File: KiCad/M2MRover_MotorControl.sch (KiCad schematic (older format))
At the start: 23 parts, among them J12 Screw_Terminal_01x02, J13 Screw_Terminal_01x02, SW1 SW_SPST, U3 L298HN

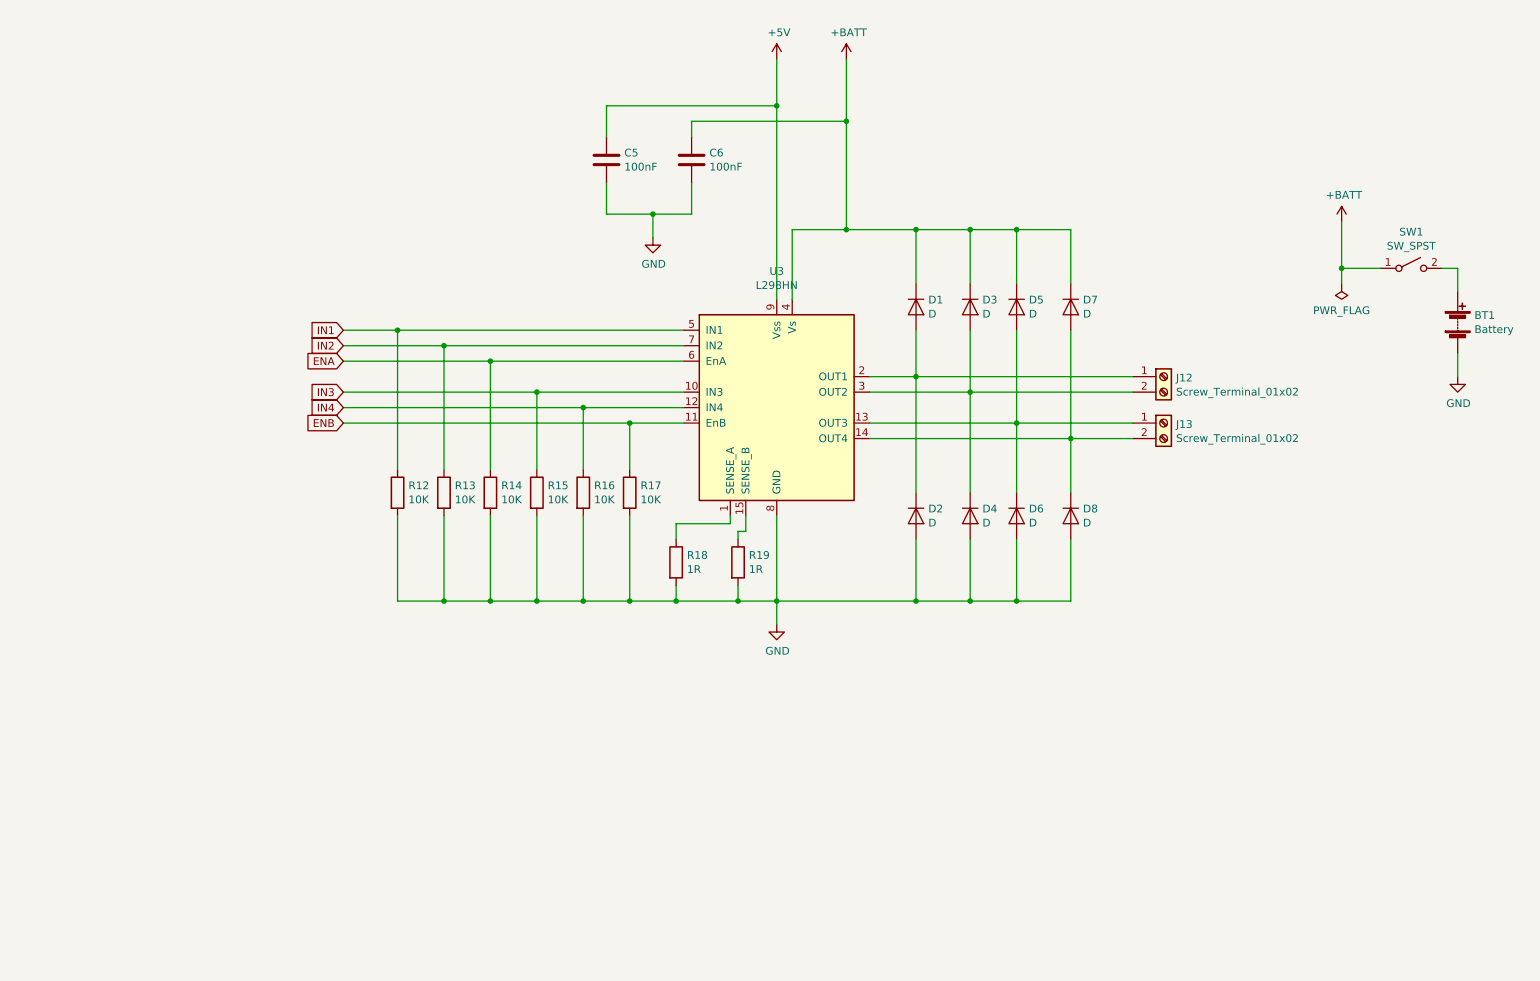
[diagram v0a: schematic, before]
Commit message: Add L298N H-Bridge driver
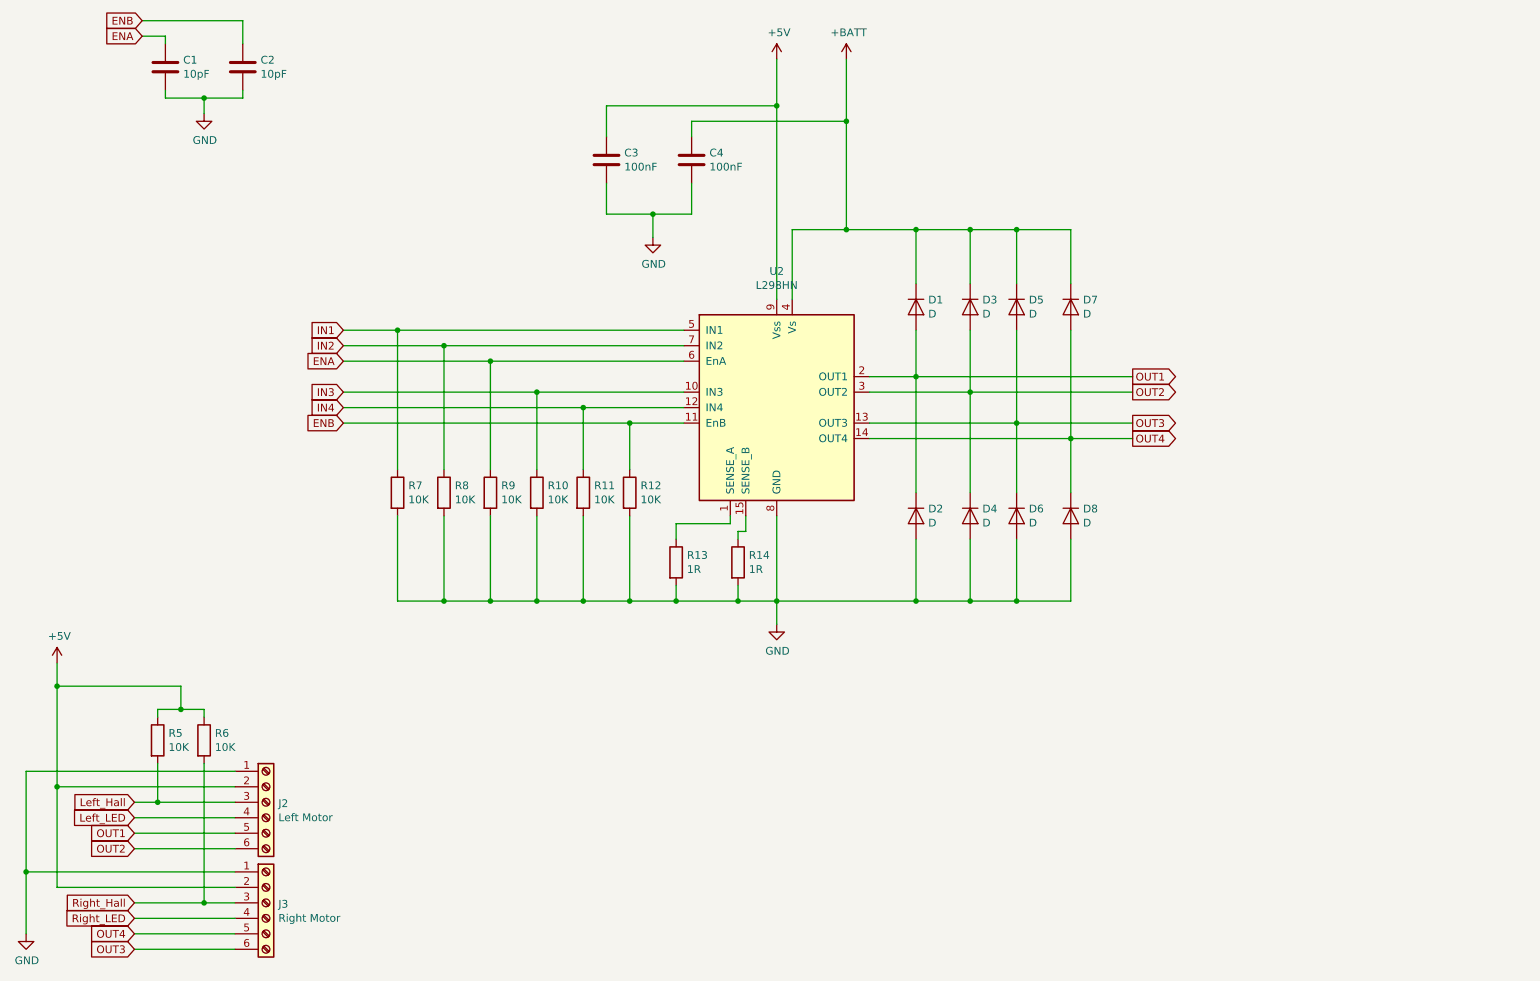
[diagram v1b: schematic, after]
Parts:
- removed BT1: Battery, symbol Device:Battery
- removed J12, J13: Screw_Terminal_01x02, symbol Connector:Screw_Terminal_01x02
- removed SW1: SW_SPST, symbol Switch:SW_SPST
- added C1, C2: 10pF, Capacitor_SMD:C_0805_2012Metric_Pad1.15x1.40mm_HandSolder, symbol Device:C
- added J2: Left Motor, Connector_PinSocket_2.54mm:PinSocket_1x06_P2.54mm_Vertical, symbol Connector:Screw_Terminal_01x06
- added J3: Right Motor, Connector_PinSocket_2.54mm:PinSocket_1x06_P2.54mm_Vertical, symbol Connector:Screw_Terminal_01x06
- added R5, R6: 10K, Resistor_SMD:R_0805_2012Metric_Pad1.15x1.40mm_HandSolder, symbol Device:R
- C3: renamed from C5; footprint (none) -> Capacitor_SMD:C_0805_2012Metric_Pad1.15x1.40mm_HandSolder
- C4: renamed from C6; footprint (none) -> Capacitor_SMD:C_0805_2012Metric_Pad1.15x1.40mm_HandSolder
- renumbered R15 to R10, R16 to R11, R17 to R12, R18 to R13, R19 to R14, R12 to R7, R13 to R8, R14 to R9, U3 to U2
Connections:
- net +5V: now also J2.2 (Pin_2), J3.2 (Pin_2), R5.1, R6.1
- net ENA: now also C1.1
- net ENB: now also C2.1
- net GND: now also C1.2, C2.2, J2.1 (Pin_1), J3.1 (Pin_1)
- net OUT3: now reaches D5.2 (A), D6.1 (K), U2.13 (OUT3)
- net OUT3: now also J3.6 (Pin_6)
- net OUT4: now reaches D7.2 (A), D8.1 (K), U2.14 (OUT4)
- net OUT4: now also J3.5 (Pin_5)
- net OUT1: now reaches D1.2 (A), D2.1 (K), U2.2 (OUT1)
- net OUT1: now also J2.5 (Pin_5)
- net OUT2: now reaches D3.2 (A), D4.1 (K), U2.3 (OUT2)
- net OUT2: now also J2.6 (Pin_6)
- new net Left_Hall: J2.3 (Pin_3), R5.2
- new net Left_LED: J2.4 (Pin_4)
- new net Right_Hall: J3.3 (Pin_3), R6.2
- new net Right_LED: J3.4 (Pin_4)

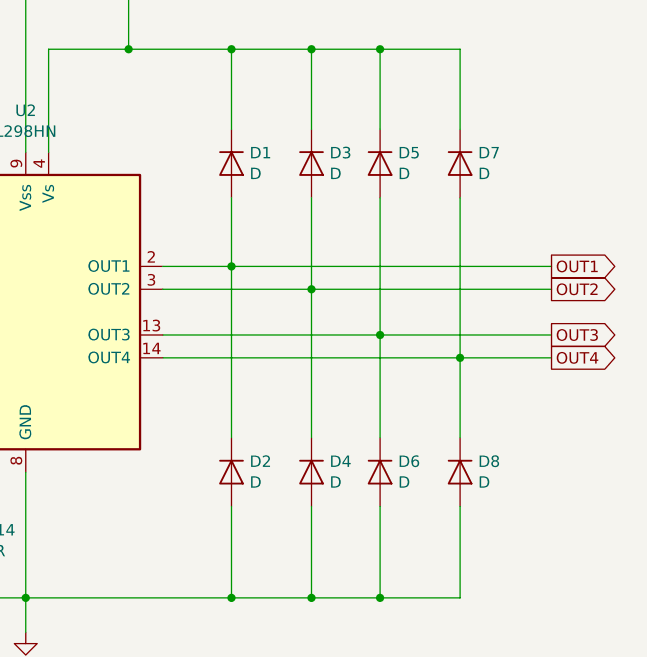
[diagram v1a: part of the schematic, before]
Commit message: Add footprints for diodes
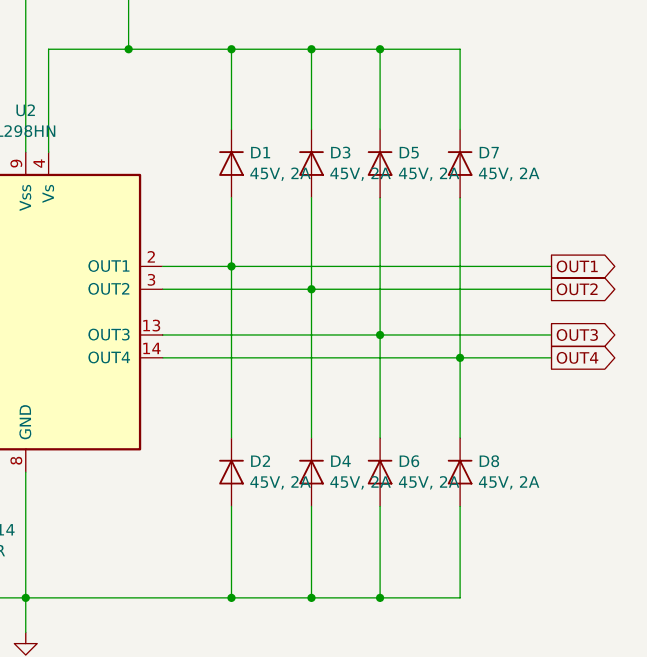
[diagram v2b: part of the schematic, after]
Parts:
- D1, D2, D3, D4, D5, D6, D7, D8: value D -> 45V, 2A; footprint (none) -> Diode_SMD:D_SOD-123
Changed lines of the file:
@@
 P 6700 2950
 F 0 "D1" V 6654 3029 50  0000 L CNN
-F 1 "D" V 6745 3029 50  0000 L CNN
-F 2 "" H 6700 2950 50  0001 C CNN
+F 1 "45V, 2A" V 6745 3029 50  0000 L CNN
+F 2 "Diode_SMD:D_SOD-123" H 6700 2950 50  0001 C CNN
 F 3 "~" H 6700 2950 50  0001 C CNN
 	1    6700 2950
@@
 P 7050 2950
 F 0 "D3" V 7004 3029 50  0000 L CNN
-F 1 "D" V 7095 3029 50  0000 L CNN
-F 2 "" H 7050 2950 50  0001 C CNN
+F 1 "45V, 2A" V 7095 3029 50  0000 L CNN
+F 2 "Diode_SMD:D_SOD-123" H 7050 2950 50  0001 C CNN
 F 3 "~" H 7050 2950 50  0001 C CNN
 	1    7050 2950
@@
 P 7350 2950
 F 0 "D5" V 7304 3029 50  0000 L CNN
-F 1 "D" V 7395 3029 50  0000 L CNN
-F 2 "" H 7350 2950 50  0001 C CNN
+F 1 "45V, 2A" V 7395 3029 50  0000 L CNN
+F 2 "Diode_SMD:D_SOD-123" H 7350 2950 50  0001 C CNN
 F 3 "~" H 7350 2950 50  0001 C CNN
 	1    7350 2950
@@
 P 7700 2950
 F 0 "D7" V 7654 3029 50  0000 L CNN
-F 1 "D" V 7745 3029 50  0000 L CNN
-F 2 "" H 7700 2950 50  0001 C CNN
+F 1 "45V, 2A" V 7745 3029 50  0000 L CNN
+F 2 "Diode_SMD:D_SOD-123" H 7700 2950 50  0001 C CNN
 F 3 "~" H 7700 2950 50  0001 C CNN
 	1    7700 2950
@@
 P 6700 4300
 F 0 "D2" V 6654 4379 50  0000 L CNN
-F 1 "D" V 6745 4379 50  0000 L CNN
-F 2 "" H 6700 4300 50  0001 C CNN
+F 1 "45V, 2A" V 6745 4379 50  0000 L CNN
+F 2 "Diode_SMD:D_SOD-123" H 6700 4300 50  0001 C CNN
 F 3 "~" H 6700 4300 50  0001 C CNN
 	1    6700 4300
@@
 P 7050 4300
 F 0 "D4" V 7004 4379 50  0000 L CNN
-F 1 "D" V 7095 4379 50  0000 L CNN
-F 2 "" H 7050 4300 50  0001 C CNN
+F 1 "45V, 2A" V 7095 4379 50  0000 L CNN
+F 2 "Diode_SMD:D_SOD-123" H 7050 4300 50  0001 C CNN
 F 3 "~" H 7050 4300 50  0001 C CNN
 	1    7050 4300
@@
 P 7350 4300
 F 0 "D6" V 7304 4379 50  0000 L CNN
-F 1 "D" V 7395 4379 50  0000 L CNN
-F 2 "" H 7350 4300 50  0001 C CNN
+F 1 "45V, 2A" V 7395 4379 50  0000 L CNN
+F 2 "Diode_SMD:D_SOD-123" H 7350 4300 50  0001 C CNN
 F 3 "~" H 7350 4300 50  0001 C CNN
 	1    7350 4300
@@
 P 7700 4300
 F 0 "D8" V 7654 4379 50  0000 L CNN
-F 1 "D" V 7745 4379 50  0000 L CNN
-F 2 "" H 7700 4300 50  0001 C CNN
+F 1 "45V, 2A" V 7745 4379 50  0000 L CNN
+F 2 "Diode_SMD:D_SOD-123" H 7700 4300 50  0001 C CNN
 F 3 "~" H 7700 4300 50  0001 C CNN
 	1    7700 4300

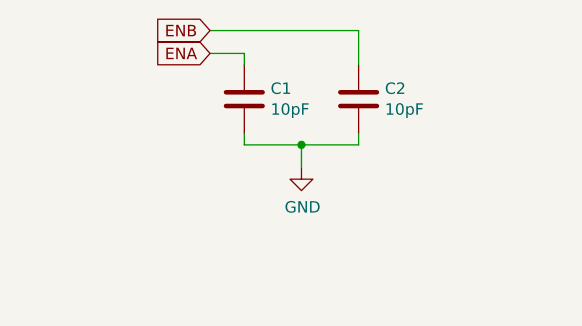
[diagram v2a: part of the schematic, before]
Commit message: Refactor motor wiring to h-bridge
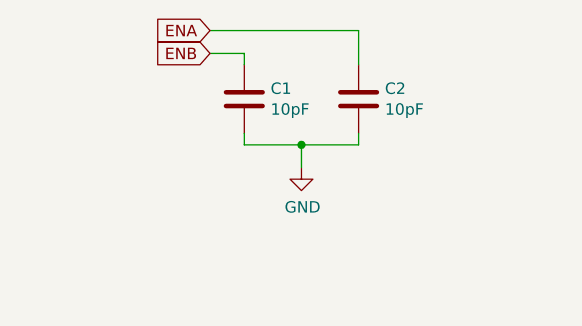
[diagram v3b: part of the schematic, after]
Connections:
- net ENA: now also C2.1; no longer C1.1
- net ENB: now also C1.1; no longer C2.1
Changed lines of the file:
@@
 $EndComp
-Wire Wire Line
-	3000 3100 3350 3100
-Wire Wire Line
-	3000 3200 3650 3200
-Wire Wire Line
-	3000 3300 3950 3300
-Wire Wire Line
-	3000 3500 4250 3500
-Wire Wire Line
-	3000 3600 4550 3600
-Wire Wire Line
-	3000 3700 4850 3700
 Wire Wire Line
 	5800 4300 5800 4850
@@
 	1    0    0    -1
 $EndComp
-Connection ~ 3350 3100
-Wire Wire Line
-	3350 3100 5200 3100
-Wire Wire Line
-	3650 4000 3650 3200
-Connection ~ 3650 3200
-Wire Wire Line
-	3650 3200 5200 3200
-Wire Wire Line
-	3950 4000 3950 3300
-Connection ~ 3950 3300
-Wire Wire Line
-	3950 3300 5200 3300
-Wire Wire Line
-	4250 4000 4250 3500
-Connection ~ 4250 3500
-Wire Wire Line
-	4250 3500 5200 3500
-Wire Wire Line
-	4550 4000 4550 3600
-Connection ~ 4550 3600
-Wire Wire Line
-	4550 3600 5200 3600
-Wire Wire Line
-	4850 4000 4850 3700
-Connection ~ 4850 3700
-Wire Wire Line
-	4850 3700 5200 3700
-Wire Wire Line
-	3350 4000 3350 3100
 $Comp
 L Device:R R7
@@
 	1850 1550 1850 1600
 Text GLabel 1700 1100 0    50   Input ~ 0
+ENA
+Text GLabel 1700 1200 0    50   Input ~ 0
 ENB
-Text GLabel 1700 1200 0    50   Input ~ 0
-ENA
 $Comp
 L Device:C C?
@@
 Wire Wire Line
 	1650 7100 2300 7100
+Wire Wire Line
+	3000 3100 3350 3100
+Wire Wire Line
+	3000 3200 3650 3200
+Wire Wire Line
+	3000 3300 3950 3300
+Wire Wire Line
+	3000 3500 4250 3500
+Wire Wire Line
+	3000 3600 4550 3600
+Wire Wire Line
+	3000 3700 4850 3700
+Wire Wire Line
+	3350 4000 3350 3100
+Connection ~ 3350 3100
+Wire Wire Line
+	3350 3100 5200 3100
+Wire Wire Line
+	3650 4000 3650 3200
+Connection ~ 3650 3200
+Wire Wire Line
+	3650 3200 5200 3200
+Wire Wire Line
+	3950 4000 3950 3300
+Connection ~ 3950 3300
+Wire Wire Line
+	3950 3300 5200 3300
+Wire Wire Line
+	4250 4000 4250 3500
+Connection ~ 4250 3500
+Wire Wire Line
+	4250 3500 5200 3500
+Wire Wire Line
+	4550 4000 4550 3600
+Connection ~ 4550 3600
+Wire Wire Line
+	4550 3600 5200 3600
+Wire Wire Line
+	4850 4000 4850 3700
+Connection ~ 4850 3700
+Wire Wire Line
+	4850 3700 5200 3700
 $EndSCHEMATC

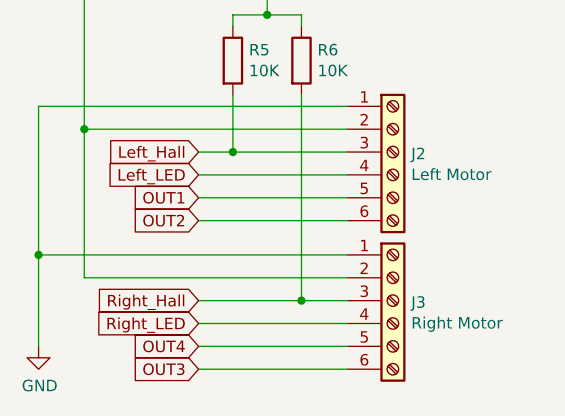
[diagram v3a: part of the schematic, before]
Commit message: Route the PCB
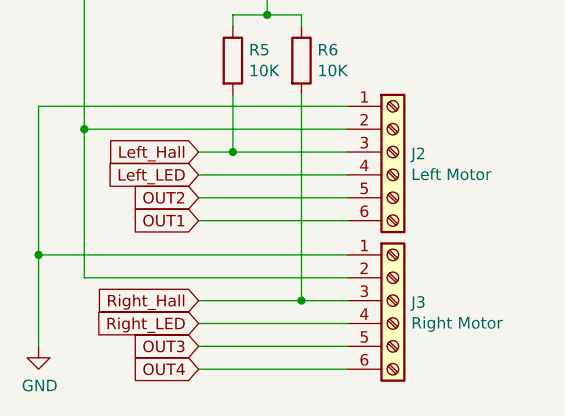
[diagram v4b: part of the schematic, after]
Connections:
- net OUT1: now also J2.6 (Pin_6); no longer J2.5 (Pin_5)
- net OUT2: now also J2.5 (Pin_5); no longer J2.6 (Pin_6)
- net OUT3: now also J3.5 (Pin_5); no longer J3.6 (Pin_6)
- net OUT4: now also J3.6 (Pin_6); no longer J3.5 (Pin_5)
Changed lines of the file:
@@
 $EndComp
 Text GLabel 1650 6350 0    50   Input ~ 0
+OUT2
+Text GLabel 1650 6450 0    50   Input ~ 0
 OUT1
-Text GLabel 1650 6450 0    50   Input ~ 0
-OUT2
 Text GLabel 1650 7100 0    50   Input ~ 0
+OUT4
+Text GLabel 1650 7000 0    50   Input ~ 0
 OUT3
-Text GLabel 1650 7000 0    50   Input ~ 0
-OUT4
 Wire Wire Line
 	1650 6350 2300 6350
